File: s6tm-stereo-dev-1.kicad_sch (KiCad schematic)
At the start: 94 parts, among them J1 Micro_SD_Card_Det1, J2 Conn_01x04_Pin, J3 USB_C_Receptacle_USB2.0_14P, SW1 SW_SPDT, SW2 SW_Push, SW3 SW_Push, SW5 SW_Push, SW6 SW_Push, SW7 RotaryEncoder_Switch, U1 ESP32-S3FN8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

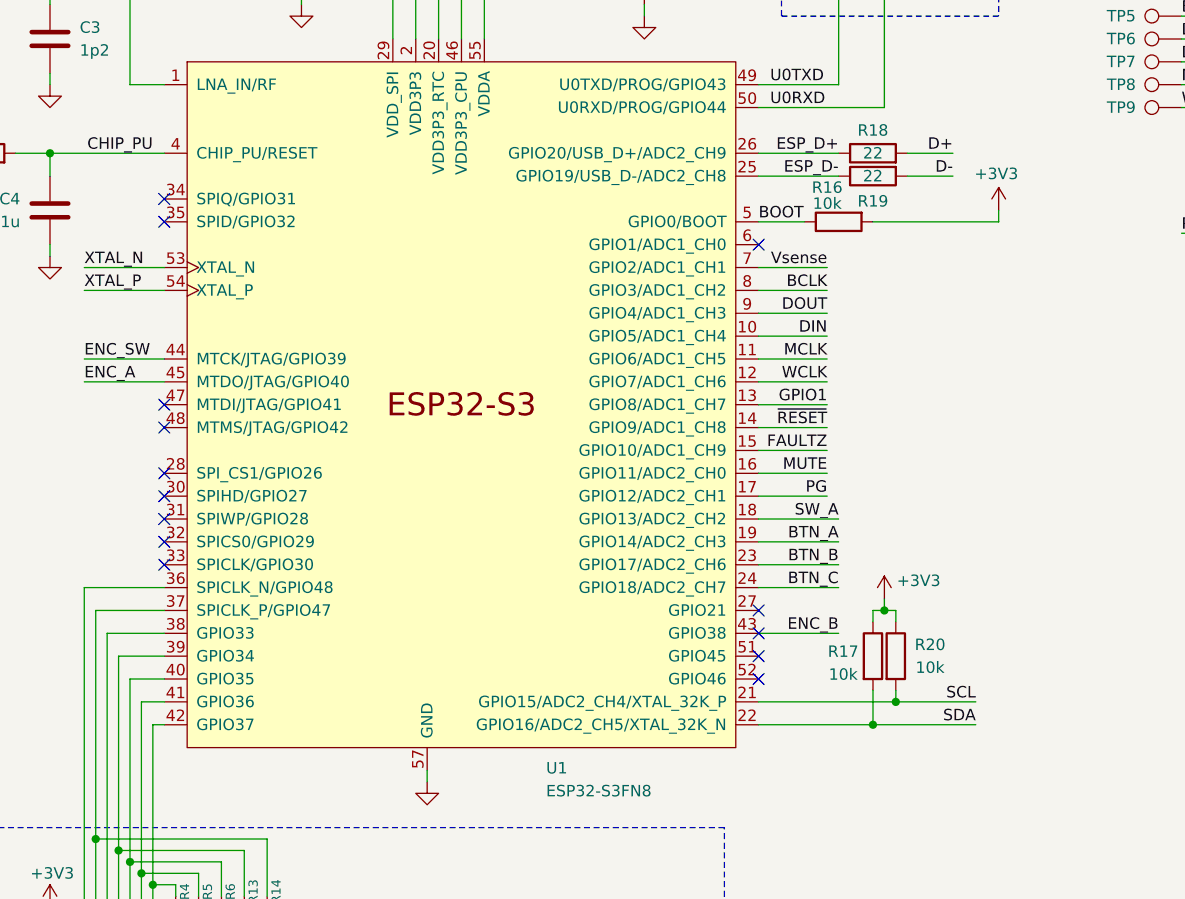
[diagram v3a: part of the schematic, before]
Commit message: pcb: add bTN_AB routing
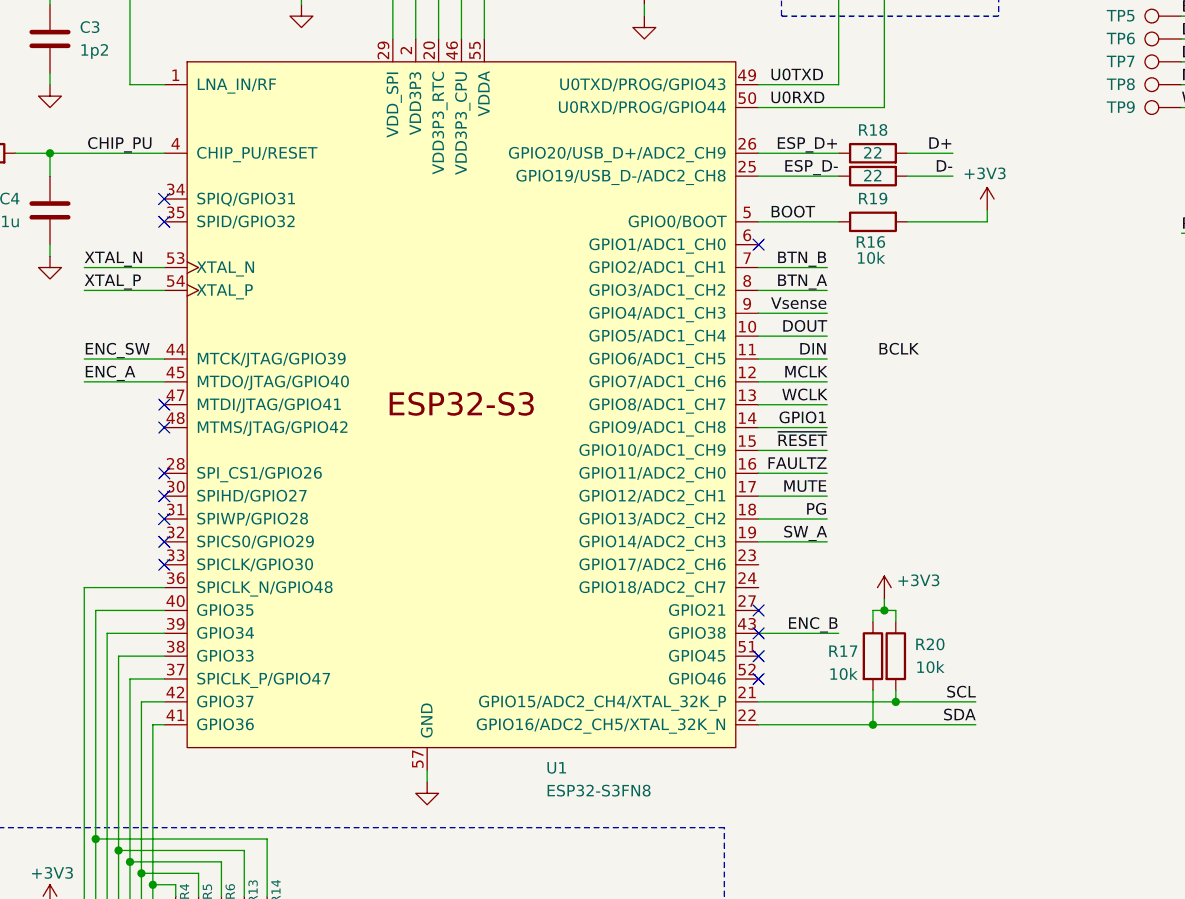
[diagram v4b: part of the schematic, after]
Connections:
- net BCLK: no longer U1.8 (GPIO3/ADC1_CH2)
- net BTN_A: now also U1.8 (GPIO3/ADC1_CH2); no longer U1.19 (GPIO14/ADC2_CH3)
- net BTN_B: now also U1.7 (GPIO2/ADC1_CH1); no longer U1.23 (GPIO17/ADC2_CH6)
- net DIN: now also U1.11 (GPIO6/ADC1_CH5); no longer U1.10 (GPIO5/ADC1_CH4)
- net DOUT: now also U1.10 (GPIO5/ADC1_CH4); no longer U1.9 (GPIO4/ADC1_CH3)
- net FAULTZ: now also U1.16 (GPIO11/ADC2_CH0); no longer U1.15 (GPIO10/ADC1_CH9)
- net GPIO1: now also U1.14 (GPIO9/ADC1_CH8); no longer U1.13 (GPIO8/ADC1_CH7)
- net MCLK: now also U1.12 (GPIO7/ADC1_CH6); no longer U1.11 (GPIO6/ADC1_CH5)
- net MUTE: now also U1.17 (GPIO12/ADC2_CH1); no longer U1.16 (GPIO11/ADC2_CH0)
- net PG: now also U1.18 (GPIO13/ADC2_CH2); no longer U1.17 (GPIO12/ADC2_CH1)
- net SW_A: now also U1.19 (GPIO14/ADC2_CH3); no longer U1.18 (GPIO13/ADC2_CH2)
- net Vsense: now also U1.9 (GPIO4/ADC1_CH3); no longer U1.7 (GPIO2/ADC1_CH1)
- net WCLK: now also U1.13 (GPIO8/ADC1_CH7); no longer U1.12 (GPIO7/ADC1_CH6)
- net ~{RESET}: now also U1.15 (GPIO10/ADC1_CH9); no longer U1.14 (GPIO9/ADC1_CH8)
- net at R10.2, R13.1: now also U1.38 (GPIO33); no longer U1.39 (GPIO34)
- net at R4.1, R7.2: now also U1.41 (GPIO36); no longer U1.42 (GPIO37)
- net at R6.1, R9.2: now also U1.37 (SPICLK_P/GPIO47); no longer U1.40 (GPIO35)
- net at R5.1, R8.2: now also U1.42 (GPIO37); no longer U1.41 (GPIO36)
- net at R12.2, R14.1: now also U1.40 (GPIO35); no longer U1.37 (SPICLK_P/GPIO47)
- net at R11.2: now also U1.39 (GPIO34); no longer U1.38 (GPIO33)
- net BTN_C: no longer names the net of U1.24 (GPIO18/ADC2_CH7)
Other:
- moved on the sheet: R16

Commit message: pcb: add Vsense and PG routing
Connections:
- net DIN: now also U1.12 (GPIO7/ADC1_CH6); no longer U1.11 (GPIO6/ADC1_CH5)
- net DOUT: now also U1.11 (GPIO6/ADC1_CH5); no longer U1.10 (GPIO5/ADC1_CH4)
- net FAULTZ: now also U1.17 (GPIO12/ADC2_CH1); no longer U1.16 (GPIO11/ADC2_CH0)
- net GPIO1: now also U1.15 (GPIO10/ADC1_CH9); no longer U1.14 (GPIO9/ADC1_CH8)
- net MCLK: now also U1.13 (GPIO8/ADC1_CH7); no longer U1.12 (GPIO7/ADC1_CH6)
- net MUTE: now also U1.18 (GPIO13/ADC2_CH2); no longer U1.17 (GPIO12/ADC2_CH1)
- net PG: now also U1.9 (GPIO4/ADC1_CH3); no longer U1.18 (GPIO13/ADC2_CH2)
- net Vsense: now also U1.10 (GPIO5/ADC1_CH4); no longer U1.9 (GPIO4/ADC1_CH3)
- net WCLK: now also U1.14 (GPIO9/ADC1_CH8); no longer U1.13 (GPIO8/ADC1_CH7)
- net ~{RESET}: now also U1.16 (GPIO11/ADC2_CH0); no longer U1.15 (GPIO10/ADC1_CH9)
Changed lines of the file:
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@@
 	(wire
 		(pts
+			(xy 134.62 102.87) (xy 127 102.87)
+		)
+		(stroke
+			(width 0)
+			(type default)
+		)
+	)
+	(wire
+		(pts
 			(xy 52.07 77.47) (xy 60.96 77.47)
 		)
@@
 	(wire
 		(pts
+			(xy 134.62 85.09) (xy 127 85.09)
+		)
+		(stroke
+			(width 0)
+			(type default)
+		)
+	)
+	(wire
+		(pts
 			(xy 45.72 186.69) (xy 45.72 187.96)
 		)
@@
 	(wire
 		(pts
-			(xy 72.39 161.29) (xy 74.93 161.29)
-		)
-		(stroke
-			(width 0)
-			(type default)
-		)
-	)
-	(wire
-		(pts
-			(xy 251.46 153.67) (xy 251.46 154.94)
+			(xy 134.62 105.41) (xy 127 105.41)
 		)
 		(stroke
@@
 	(wire
 		(pts
-			(xy 134.62 90.17) (xy 127 90.17)
+			(xy 72.39 161.29) (xy 74.93 161.29)
 		)
 		(stroke
@@
 	(wire
 		(pts
-			(xy 134.62 105.41) (xy 127 105.41)
+			(xy 251.46 153.67) (xy 251.46 154.94)
 		)
 		(stroke
@@
 	(wire
 		(pts
+			(xy 134.62 92.71) (xy 127 92.71)
+		)
+		(stroke
+			(width 0)
+			(type default)
+		)
+	)
+	(wire
+		(pts
 			(xy 48.26 55.88) (xy 48.26 57.15)
 		)
@@
 	(wire
 		(pts
-			(xy 134.62 100.33) (xy 127 100.33)
-		)
-		(stroke
-			(width 0)
-			(type default)
-		)
-	)
-	(wire
-		(pts
 			(xy 276.86 127) (xy 275.59 127)
 		)
@@
 	(wire
 		(pts
-			(xy 134.62 85.09) (xy 127 85.09)
-		)
-		(stroke
-			(width 0)
-			(type default)
-		)
-	)
-	(wire
-		(pts
-			(xy 134.62 97.79) (xy 127 97.79)
+			(xy 21.59 185.42) (xy 21.59 184.15)
 		)
 		(stroke
@@
 	(wire
 		(pts
-			(xy 21.59 185.42) (xy 21.59 184.15)
+			(xy 134.62 87.63) (xy 127 87.63)
 		)
 		(stroke
@@
 	(wire
 		(pts
-			(xy 134.62 102.87) (xy 127 102.87)
+			(xy 62.23 146.05) (xy 59.69 146.05)
 		)
 		(stroke
@@
 	(wire
 		(pts
-			(xy 62.23 146.05) (xy 59.69 146.05)
+			(xy 106.68 21.59) (xy 106.68 22.86)
 		)
 		(stroke
@@
 	(wire
 		(pts
-			(xy 106.68 21.59) (xy 106.68 22.86)
+			(xy 53.34 140.97) (xy 72.39 140.97)
 		)
 		(stroke
@@
 	(wire
 		(pts
-			(xy 53.34 140.97) (xy 72.39 140.97)
+			(xy 134.62 97.79) (xy 127 97.79)
 		)
 		(stroke
@@
 	(wire
 		(pts
-			(xy 134.62 87.63) (xy 127 87.63)
-		)
-		(stroke
-			(width 0)
-			(type default)
-		)
-	)
-	(wire
-		(pts
 			(xy 69.85 157.48) (xy 72.39 157.48)
 		)
@@
 	(wire
 		(pts
+			(xy 134.62 90.17) (xy 127 90.17)
+		)
+		(stroke
+			(width 0)
+			(type default)
+		)
+	)
+	(wire
+		(pts
 			(xy 143.51 180.34) (xy 144.78 180.34)
 		)
@@
 	(wire
 		(pts
+			(xy 134.62 100.33) (xy 127 100.33)
+		)
+		(stroke
+			(width 0)
+			(type default)
+		)
+	)
+	(wire
+		(pts
 			(xy 58.42 163.83) (xy 64.77 163.83)
 		)
@@
 	(wire
 		(pts
-			(xy 134.62 92.71) (xy 127 92.71)
-		)
-		(stroke
-			(width 0)
-			(type default)
-		)
-	)
-	(wire
-		(pts
 			(xy 152.4 71.12) (xy 152.4 72.39)
 		)
@@
 	(wire
 		(pts
+			(xy 134.62 95.25) (xy 127 95.25)
+		)
+		(stroke
+			(width 0)
+			(type default)
+		)
+	)
+	(wire
+		(pts
 			(xy 77.47 21.59) (xy 78.74 21.59)
 		)
@@
 	(wire
 		(pts
-			(xy 134.62 95.25) (xy 127 95.25)
-		)
-		(stroke
-			(width 0)
-			(type default)
-		)
-	)
-	(wire
-		(pts
 			(xy 55.88 120.65) (xy 55.88 142.24)
 		)
@@
 		)
 	)
-	(label "BTN_A"
-		(at 217.17 114.3 180)
+	(label "DOUT"
+		(at 134.62 87.63 180)
 		(effects
 			(font
@@
 		)
 	)
-	(label "DOUT"
-		(at 134.62 85.09 180)
+	(label "PG"
+		(at 134.62 82.55 180)
+		(effects
+			(font
+				(size 1.27 1.27)
+			)
+			(justify right bottom)
+		)
+	)
+	(label "BTN_A"
+		(at 217.17 114.3 180)
 		(effects
 			(font
@@
 		)
 	)
+	(label "MUTE"
+		(at 134.62 105.41 180)
+		(effects
+			(font
+				(size 1.27 1.27)
+			)
+			(justify right bottom)
+		)
+	)
 	(label "SW_A"
 		(at 217.17 105.41 180)
@@
 		)
 	)
-	(label "~{RESET}"
-		(at 134.62 97.79 180)
+	(label "Vsense"
+		(at 134.62 85.09 180)
 		(effects
 			(font
@@
 		)
 	)
+	(label "DIN"
+		(at 134.62 90.17 180)
+		(effects
+			(font
+				(size 1.27 1.27)
+			)
+			(justify right bottom)
+		)
+	)
 	(label "ENC_B"
 		(at 247.65 38.1 0)
@@
 		)
 	)
-	(label "PG"
-		(at 134.62 105.41 180)
-		(effects
-			(font
-				(size 1.27 1.27)
-			)
-			(justify right bottom)
-		)
-	)
-	(label "ESP_D+"
-		(at 135.89 64.77 180)
+	(label "~{RESET}"
+		(at 134.62 100.33 180)
 		(effects
 			(font
@@
 		)
 	)
-	(label "CHIP_PU"
-		(at 217.17 129.54 180)
+	(label "GPIO1"
+		(at 134.62 97.79 180)
 		(effects
 			(font
@@
 		)
 	)
-	(label "MCLK"
-		(at 134.62 90.17 180)
+	(label "ESP_D+"
+		(at 135.89 64.77 180)
 		(effects
 			(font
@@
 		)
 	)
-	(label "FAULTZ"
-		(at 134.62 100.33 180)
+	(label "CHIP_PU"
+		(at 217.17 129.54 180)
 		(effects
 			(font
@@
 		)
 	)
-	(label "MUTE"
-		(at 134.62 102.87 180)
-		(effects
-			(font
-				(size 1.27 1.27)
-			)
-			(justify right bottom)
-		)
-	)
 	(label "WCLK"
 		(at 173.99 59.69 0)
@@
 		)
 	)
-	(label "WCLK"
-		(at 134.62 92.71 180)
-		(effects
-			(font
-				(size 1.27 1.27)
-			)
-			(justify right bottom)
-		)
-	)
 	(label "Vsense"
 		(at 182.88 146.05 0)
@@
 		)
 	)
+	(label "MCLK"
+		(at 134.62 92.71 180)
+		(effects
+			(font
+				(size 1.27 1.27)
+			)
+			(justify right bottom)
+		)
+	)
 	(label "RF_ESP"
 		(at 49.53 45.72 0)
@@
 		)
 	)
-	(label "GPIO1"
-		(at 134.62 95.25 180)
-		(effects
-			(font
-				(size 1.27 1.27)
-			)
-			(justify right bottom)
-		)
-	)
-	(label "Vsense"
-		(at 134.62 82.55 180)
-		(effects
-			(font
-				(size 1.27 1.27)
-			)
-			(justify right bottom)
-		)
-	)
 	(label "SDA"
 		(at 173.99 41.91 0)
@@
 		)
 	)
+	(label "WCLK"
+		(at 134.62 95.25 180)
+		(effects
+			(font
+				(size 1.27 1.27)
+			)
+			(justify right bottom)
+		)
+	)
 	(label "ENC_A"
 		(at 247.65 33.02 0)
@@
 		)
 	)
-	(label "DIN"
-		(at 134.62 87.63 180)
+	(label "FAULTZ"
+		(at 134.62 102.87 180)
 		(effects
 			(font

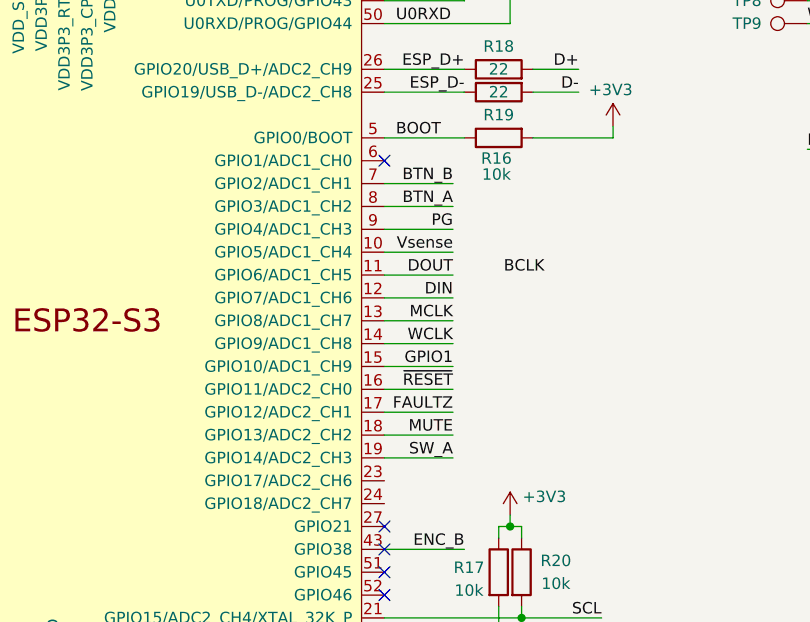
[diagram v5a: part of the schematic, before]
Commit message: pcb: add SW_A routing
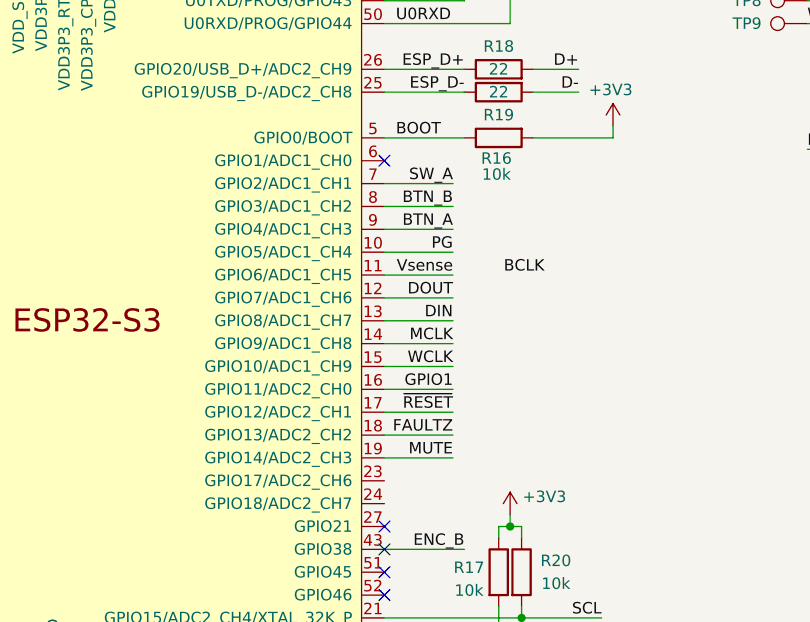
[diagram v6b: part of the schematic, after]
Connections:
- net BTN_A: now also U1.9 (GPIO4/ADC1_CH3); no longer U1.8 (GPIO3/ADC1_CH2)
- net BTN_B: now also U1.8 (GPIO3/ADC1_CH2); no longer U1.7 (GPIO2/ADC1_CH1)
- net DIN: now also U1.13 (GPIO8/ADC1_CH7); no longer U1.12 (GPIO7/ADC1_CH6)
- net DOUT: now also U1.12 (GPIO7/ADC1_CH6); no longer U1.11 (GPIO6/ADC1_CH5)
- net FAULTZ: now also U1.18 (GPIO13/ADC2_CH2); no longer U1.17 (GPIO12/ADC2_CH1)
- net GPIO1: now also U1.16 (GPIO11/ADC2_CH0); no longer U1.15 (GPIO10/ADC1_CH9)
- net MCLK: now also U1.14 (GPIO9/ADC1_CH8); no longer U1.13 (GPIO8/ADC1_CH7)
- net MUTE: now also U1.19 (GPIO14/ADC2_CH3); no longer U1.18 (GPIO13/ADC2_CH2)
- net PG: now also U1.10 (GPIO5/ADC1_CH4); no longer U1.9 (GPIO4/ADC1_CH3)
- net SW_A: now also U1.7 (GPIO2/ADC1_CH1); no longer U1.19 (GPIO14/ADC2_CH3)
- net Vsense: now also U1.11 (GPIO6/ADC1_CH5); no longer U1.10 (GPIO5/ADC1_CH4)
- net WCLK: now also U1.15 (GPIO10/ADC1_CH9); no longer U1.14 (GPIO9/ADC1_CH8)
- net ~{RESET}: now also U1.17 (GPIO12/ADC2_CH1); no longer U1.16 (GPIO11/ADC2_CH0)

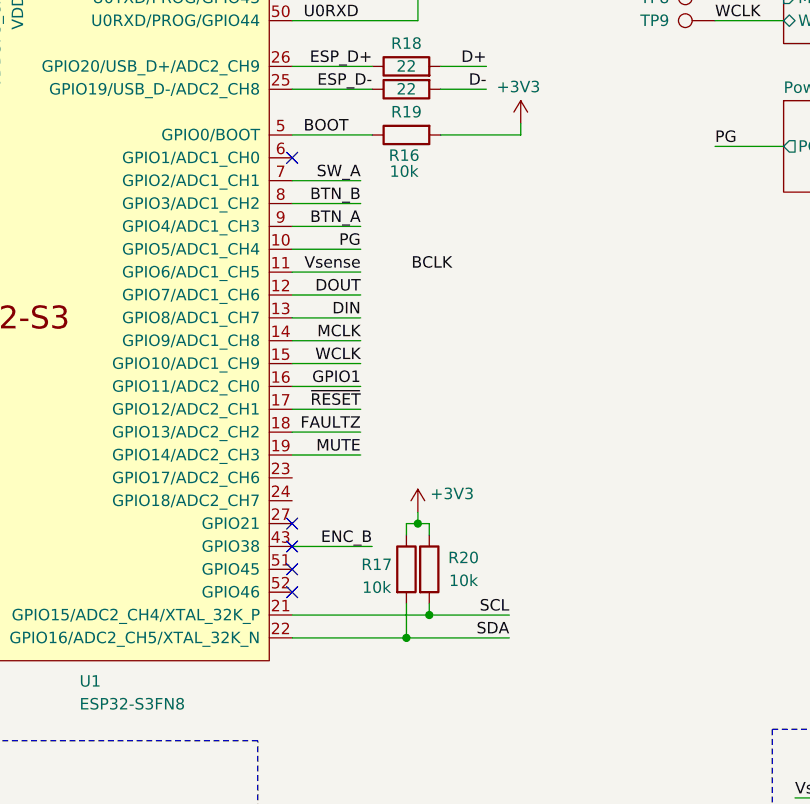
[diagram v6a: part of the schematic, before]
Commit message: pcb: add I2C routing
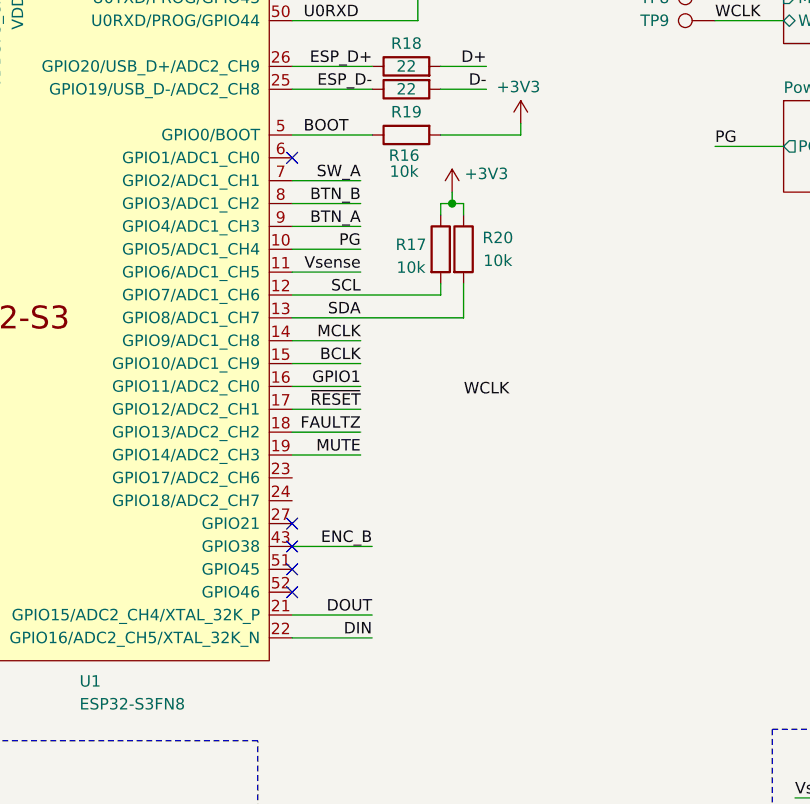
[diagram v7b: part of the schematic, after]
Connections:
- net BCLK: now also U1.15 (GPIO10/ADC1_CH9)
- net DIN: now also U1.22 (GPIO16/ADC2_CH5/XTAL_32K_N); no longer U1.13 (GPIO8/ADC1_CH7)
- net DOUT: now also U1.21 (GPIO15/ADC2_CH4/XTAL_32K_P); no longer U1.12 (GPIO7/ADC1_CH6)
- net SCL: now also R17.2, U1.12 (GPIO7/ADC1_CH6); no longer R20.2, U1.21 (GPIO15/ADC2_CH4/XTAL_32K_P)
- net SDA: now also R20.2, U1.13 (GPIO8/ADC1_CH7); no longer R17.2, U1.22 (GPIO16/ADC2_CH5/XTAL_32K_N)
- net WCLK: no longer U1.15 (GPIO10/ADC1_CH9)
